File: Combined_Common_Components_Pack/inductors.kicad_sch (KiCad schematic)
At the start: 3 parts

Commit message: Added some connectors and basic parts
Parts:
- added L8: 33u, Inductor_SMD:L_APV_APH0630, symbol Device:L
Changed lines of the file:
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@@
+	(symbol
+		(lib_id "Device:L")
+		(at 105.41 38.1 90)
+		(unit 1)
+		(exclude_from_sim no)
+		(in_bom yes)
+		(on_board yes)
+		(dnp no)
+		(property "Reference" "L8"
+			(at 105.41 33.02 90)
+			(effects
+				(font
+					(size 1.27 1.27)
+				)
+			)
+		)
+		(property "Value" "33u"
+			(at 105.41 35.56 90)
+			(effects
+				(font
+					(size 1.27 1.27)
+				)
+			)
+		)
+		(property "Footprint" "Inductor_SMD:L_APV_APH0630"
+			(at 105.41 38.1 0)
+			(effects
+				(font
+					(size 1.27 1.27)
+				)
+				(hide yes)
+			)
+		)
+		(property "Datasheet" "https://www.lcsc.com/datasheet/C5349702.pdf"
+			(at 105.41 38.1 0)
+			(effects
+				(font
+					(size 1.27 1.27)
+				)
+				(hide yes)
+			)
+		)
+		(property "Description" "2.5A 22uH 170mΩ 3A Molded Inductor ±20% SMD,7x6.6mm Fixed Inductors RoHS"
+			(at 105.41 38.1 0)
+			(effects
+				(font
+					(size 1.27 1.27)
+				)
+				(hide yes)
+			)
+		)
+		(property "LCSC" "C5349702"
+			(at 105.41 38.1 90)
+			(effects
+				(font
+					(size 1.27 1.27)
+				)
+				(hide yes)
+			)
+		)
+		(property "Observations" "2A 10.5x10.5mm"
+			(at 105.41 39.878 90)
+			(effects
+				(font
+					(size 1.27 1.27)
+				)
+			)
+		)
+		(pin "1"
+		)
+		(pin "2"
+		)
+		(instances
+			(project "Combined_Common_Components_Pack"
+				(path "/59e42e8e-5444-465a-b7a8-ffbd342a8d49/f54435ba-8a19-494c-86c3-07289aa1e26f"
+					(reference "L8")
+					(unit 1)
+				)
+			)
+		)
+	)
 	(symbol
 		(lib_id "Device:L")

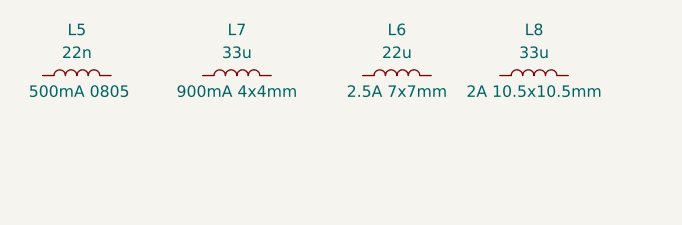
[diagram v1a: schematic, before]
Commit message: Minor updates
Basically components annotation, and more basic parts added
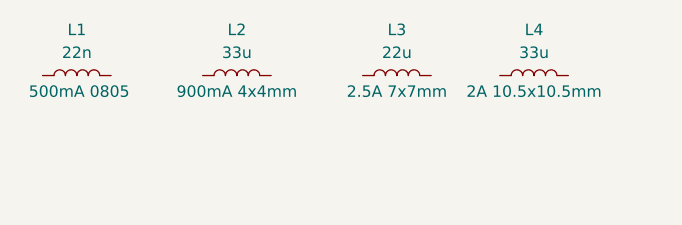
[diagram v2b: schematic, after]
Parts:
- renumbered L5 to L1, L7 to L2, L6 to L3, L8 to L4
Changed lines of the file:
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@@
 		(on_board yes)
 		(dnp no)
-		(property "Reference" "L8"
+		(property "Reference" "L4"
 			(at 105.41 33.02 90)
 			(effects
@@
 			(project "Combined_Common_Components_Pack"
 				(path "/59e42e8e-5444-465a-b7a8-ffbd342a8d49/f54435ba-8a19-494c-86c3-07289aa1e26f"
-					(reference "L8")
+					(reference "L4")
 					(unit 1)
 				)
@@
 		(on_board yes)
 		(dnp no)
-		(property "Reference" "L6"
+		(property "Reference" "L3"
 			(at 90.17 33.02 90)
 			(effects
@@
 			(project "Combined_Common_Components_Pack"
 				(path "/59e42e8e-5444-465a-b7a8-ffbd342a8d49/f54435ba-8a19-494c-86c3-07289aa1e26f"
-					(reference "L6")
+					(reference "L3")
 					(unit 1)
 				)
@@
 		(on_board yes)
 		(dnp no)
-		(property "Reference" "L5"
+		(property "Reference" "L1"
 			(at 54.61 33.02 90)
 			(effects
@@
 			(project "Combined_Common_Components_Pack"
 				(path "/59e42e8e-5444-465a-b7a8-ffbd342a8d49/f54435ba-8a19-494c-86c3-07289aa1e26f"
-					(reference "L5")
+					(reference "L1")
 					(unit 1)
 				)
@@
 		(on_board yes)
 		(dnp no)
-		(property "Reference" "L7"
+		(property "Reference" "L2"
 			(at 72.39 33.02 90)
 			(effects
@@
 			(project "Combined_Common_Components_Pack"
 				(path "/59e42e8e-5444-465a-b7a8-ffbd342a8d49/f54435ba-8a19-494c-86c3-07289aa1e26f"
-					(reference "L7")
+					(reference "L2")
 					(unit 1)
 				)

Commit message: Minor updates
Started footprint library for easier cross-computer design management.
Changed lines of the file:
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@@
 (kicad_sch
-	(version 20231120)
+	(version 20250114)
 	(generator "eeschema")
-	(generator_version "8.0")
+	(generator_version "9.0")
 	(paper "A4")
 	(symbol

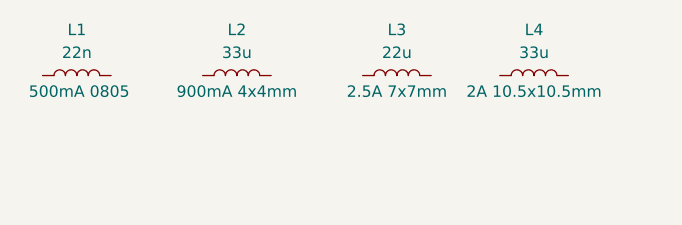
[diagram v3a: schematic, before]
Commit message: Added XL4001 Load limiter devboard
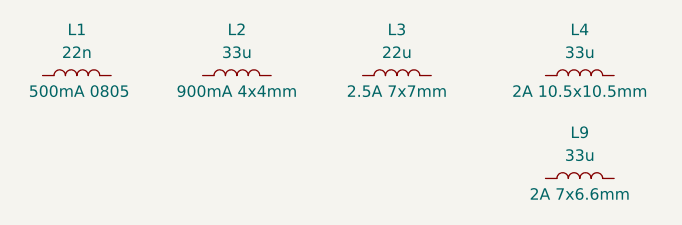
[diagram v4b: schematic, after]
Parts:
- added L9: 33u, Inductor_SMD:L_Chilisin_BMRx00060630, symbol Device:L
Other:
- moved on the sheet: L4
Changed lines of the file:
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@@
 	(symbol
 		(lib_id "Device:L")
-		(at 105.41 38.1 90)
+		(at 110.49 49.53 90)
 		(unit 1)
 		(exclude_from_sim no)
@@
 		(on_board yes)
 		(dnp no)
-		(property "Reference" "L4"
-			(at 105.41 33.02 90)
+		(property "Reference" "L9"
+			(at 110.49 44.45 90)
 			(effects
 				(font
@@
 		)
 		(property "Value" "33u"
-			(at 105.41 35.56 90)
+			(at 110.49 46.99 90)
+			(effects
+				(font
+					(size 1.27 1.27)
+				)
+			)
+		)
+		(property "Footprint" "Inductor_SMD:L_Chilisin_BMRx00060630"
+			(at 110.49 49.53 0)
+			(effects
+				(font
+					(size 1.27 1.27)
+				)
+				(hide yes)
+			)
+		)
+		(property "Datasheet" "https://www.lcsc.com/datasheet/C177245.pdf?spm=wm.sxq.inf.ggs___wm.fly.bg.0.xh&lcsc_vid=RlVdUVxWFlBWBgBWFgRfUFIATlFaBlVTT1QLUFRXQwAxVlNRQFhbV1VST1VfUDsOAxUeFF5JWBYZEEoKFBINSQcJGk4eFQsCAgIaSgADAwAHC0slRVZYV1ZfRE8GEwkK"
+			(at 110.49 49.53 0)
+			(effects
+				(font
+					(size 1.27 1.27)
+				)
+				(hide yes)
+			)
+		)
+		(property "Description" "2A 33uH ±20% 2.5A 310mΩ Molded Inductor SMD,7x6.6mm Fixed Inductors RoHS"
+			(at 110.49 49.53 0)
+			(effects
+				(font
+					(size 1.27 1.27)
+				)
+				(hide yes)
+			)
+		)
+		(property "LCSC" "C177245"
+			(at 110.49 49.53 90)
+			(effects
+				(font
+					(size 1.27 1.27)
+				)
+				(hide yes)
+			)
+		)
+		(property "Observations" "2A 7x6.6mm"
+			(at 110.49 51.308 90)
+			(effects
+				(font
+					(size 1.27 1.27)
+				)
+			)
+		)
+		(pin "1"
+		)
+		(pin "2"
+		)
+		(instances
+			(project "Combined_Common_Components_Pack"
+				(path "/59e42e8e-5444-465a-b7a8-ffbd342a8d49/f54435ba-8a19-494c-86c3-07289aa1e26f"
+					(reference "L9")
+					(unit 1)
+				)
+			)
+		)
+	)
+	(symbol
+		(lib_id "Device:L")
+		(at 110.49 38.1 90)
+		(unit 1)
+		(exclude_from_sim no)
+		(in_bom yes)
+		(on_board yes)
+		(dnp no)
+		(property "Reference" "L4"
+			(at 110.49 33.02 90)
+			(effects
+				(font
+					(size 1.27 1.27)
+				)
+			)
+		)
+		(property "Value" "33u"
+			(at 110.49 35.56 90)
 			(effects
 				(font
@@
 		)
 		(property "Footprint" "Inductor_SMD:L_APV_APH0630"
-			(at 105.41 38.1 0)
+			(at 110.49 38.1 0)
 			(effects
 				(font
@@
 		)
 		(property "Datasheet" "https://www.lcsc.com/datasheet/C5349702.pdf"
-			(at 105.41 38.1 0)
+			(at 110.49 38.1 0)
 			(effects
 				(font
@@
 		)
 		(property "Description" "2.5A 22uH 170mΩ 3A Molded Inductor ±20% SMD,7x6.6mm Fixed Inductors RoHS"
-			(at 105.41 38.1 0)
+			(at 110.49 38.1 0)
 			(effects
 				(font
@@
 		)
 		(property "LCSC" "C5349702"
-			(at 105.41 38.1 90)
+			(at 110.49 38.1 90)
 			(effects
 				(font
@@
 		)
 		(property "Observations" "2A 10.5x10.5mm"
-			(at 105.41 39.878 90)
+			(at 110.49 39.878 90)
 			(effects
 				(font
